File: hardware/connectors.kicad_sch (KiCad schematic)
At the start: 4 parts, among them J1 74650073R, J4 Conn_01x06, J5 UMPT-08-01-L-RA-WT-P-TR, J8 UMPT-08-01-L-RA-WT-P-TR

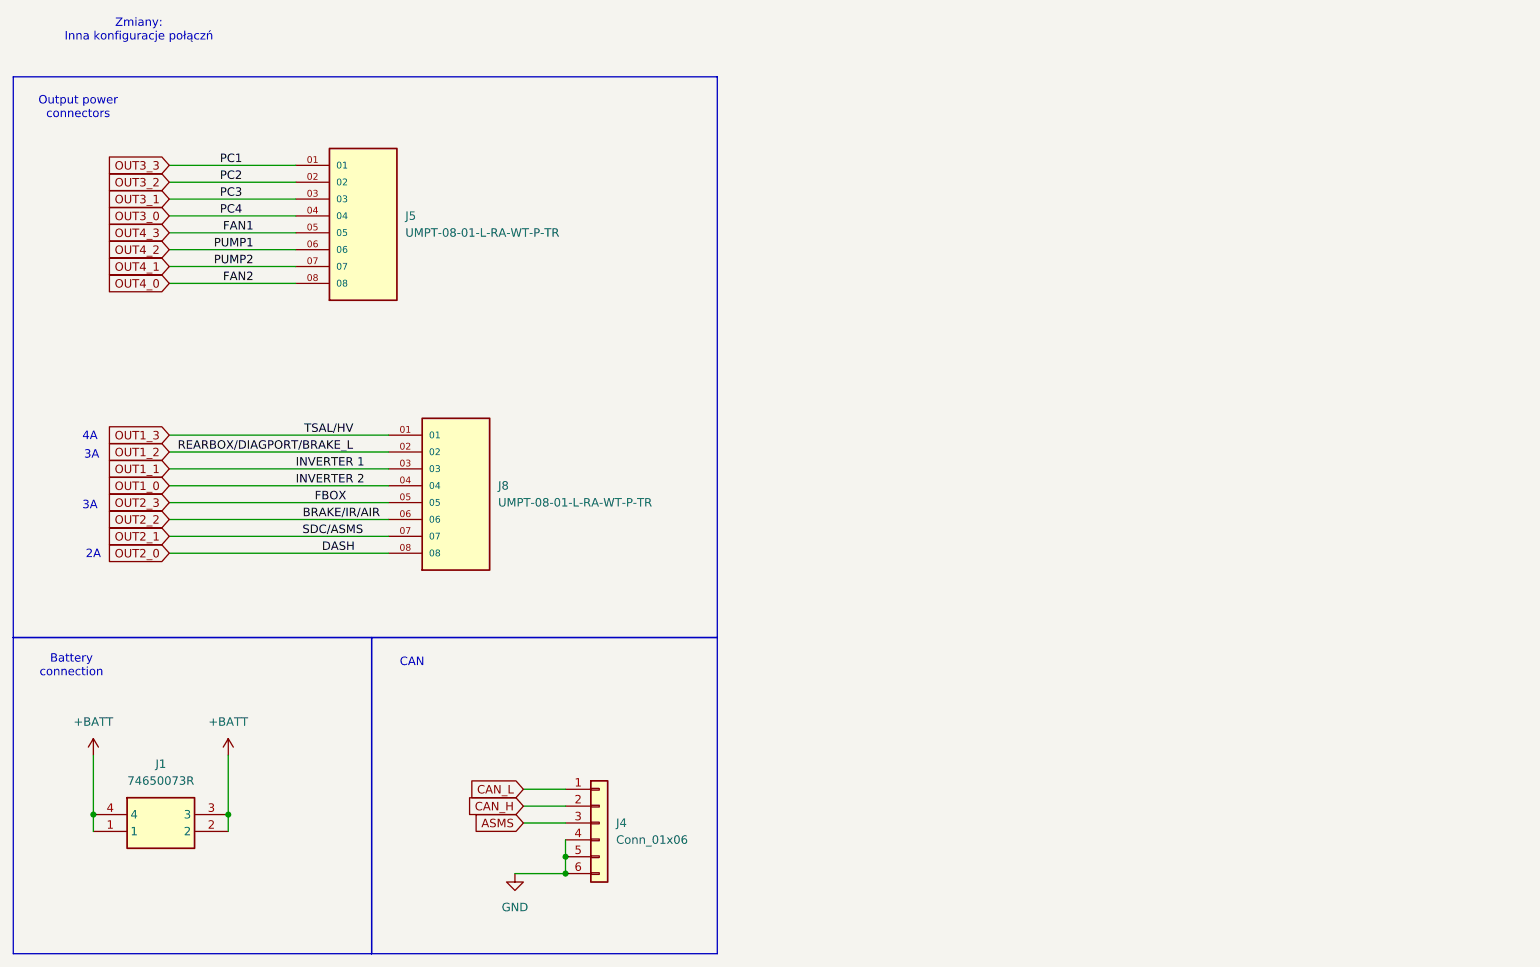
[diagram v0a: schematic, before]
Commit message: cube->cmake port, current calc fix, spi datalength fix, hard-v1.1.0 sync
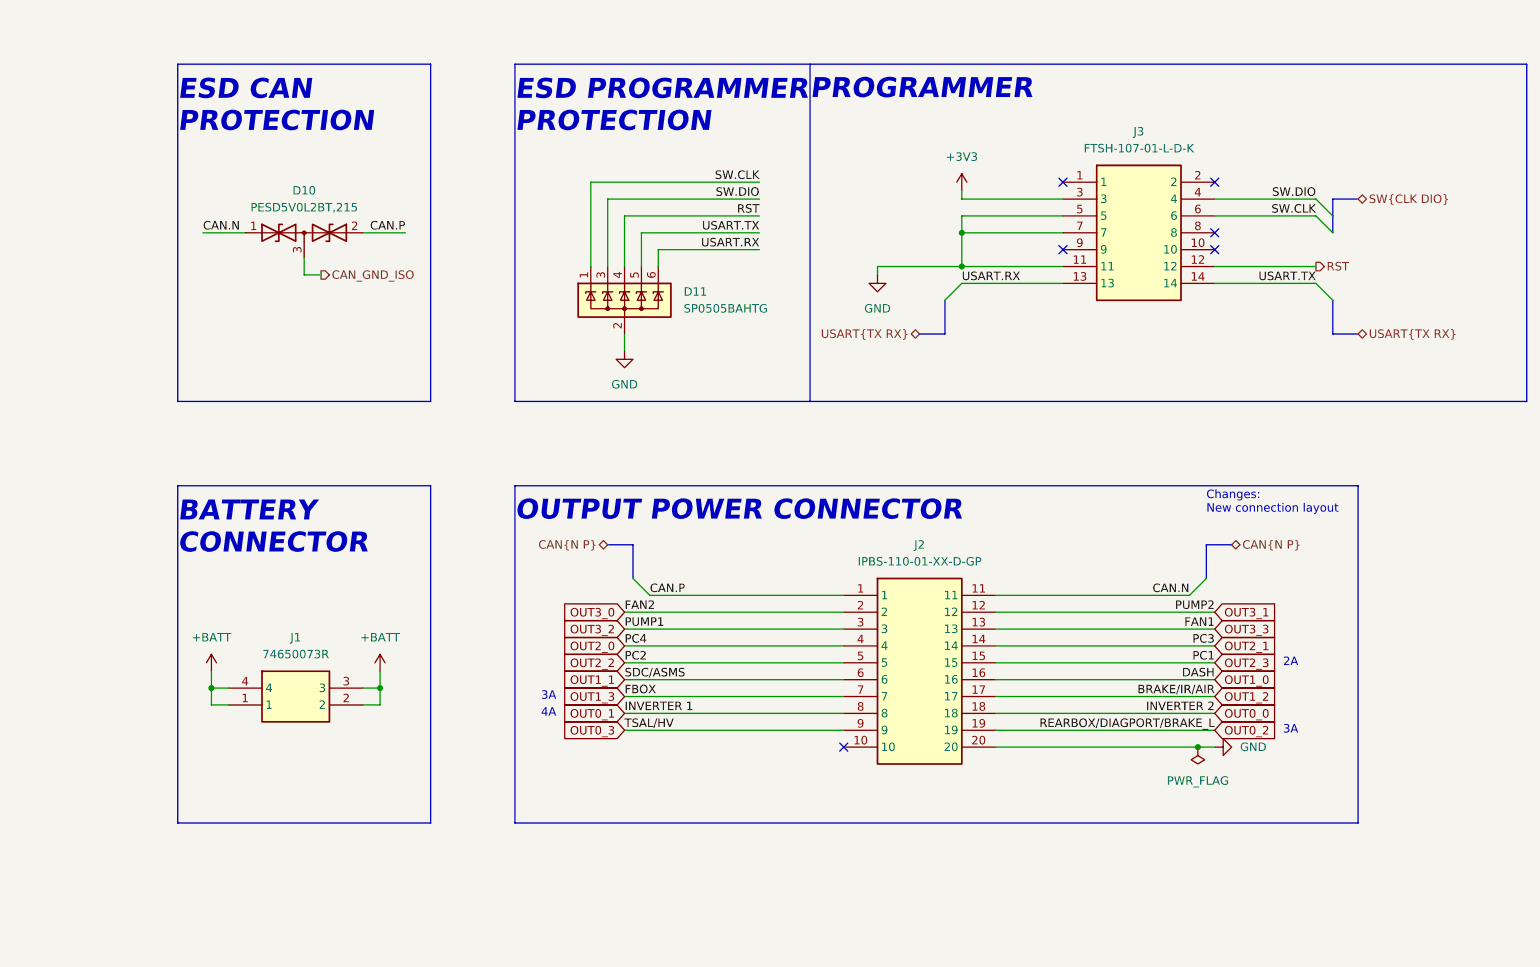
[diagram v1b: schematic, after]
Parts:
- removed J4: Conn_01x06, Connector_IDC:IDC-Header_2x03_P2.54mm_Vertical, symbol Connector_Generic:Conn_01x06
- removed J5, J8: UMPT-08-01-L-RA-WT-P-TR, UMPT-08-01-L-RA-WT-P-TR:SAMTEC_UMPT-08-01-L-RA-WT-P-TR, symbol UMPT-08-01-L-RA-WT-P-TR:UMPT-08-01-L-RA-WT-P-TR
- added D10: PESD5V0L2BT,215, Package_TO_SOT_SMD:SOT-23-3, symbol Device:D_TVS_Dual_AAC
- added D11: SP0505BAHTG, Package_TO_SOT_SMD:SOT-23-6_Handsoldering, symbol Power_Protection:SP0505BAHT
- added J2: IPBS-110-01-XX-D-GP, PDM:IPBT110H1TDRAGP, symbol PDM:IPBS-110-01-T-D-GP
- added J3: FTSH-107-01-L-D-K, PDM:FTSH-107-XX-YYY-D-K, symbol PDM:FTSH-107-01-L-D-K
- J1: footprint 74650073R -> PDM:74650073R; symbol Redcube_conn:74650073R -> PDM:74650073R; Done? (none) -> y
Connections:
- net GND: now also D11.2 (A), J2.20, J3.11, J3.5, J3.7
- net OUT1_0: now also J2.16
- net OUT1_1: now also J2.6
- net OUT1_2: now also J2.17
- net OUT1_3: now also J2.7
- net OUT2_0: now also J2.4
- net OUT2_1: now also J2.14
- net OUT2_2: now also J2.5
- net OUT2_3: now also J2.15
- net OUT3_0: now also J2.2
- net OUT3_1: now also J2.12
- net OUT3_2: now also J2.3
- net OUT3_3: now also J2.13
- new net +3V3: J3.3
- new net CAN.N: D10.1 (A1), J2.11
- new net CAN.P: D10.2 (A2), J2.1
- new net CAN_GND_ISO: D10.3 (common)
- new net OUT0_0: J2.18
- new net OUT0_1: J2.8
- new net OUT0_2: J2.19
- new net OUT0_3: J2.9
- new net RST: D11.4 (K), J3.12
- new net SW.CLK: D11.1 (K), J3.6
- new net SW.DIO: D11.3 (K), J3.4
- new net USART.RX: D11.6 (K), J3.13
- new net USART.TX: D11.5 (K), J3.14
- no-connect marks 0 -> 6
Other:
- note added: "BATTERY CONNECTOR"
- note added: "Changes: New connection layout"
- note added: "ESD CAN PROTECTION"
- note added: "ESD PROGRAMMER PROTECTION"
- note added: "OUTPUT POWER CONNECTOR"
- note added: "PROGRAMMER"
- note removed: "Battery connection"
- note removed: "CAN"
- note removed: "Output power connectors"
- note removed: "Zmiany: Inna konfiguracje połączń"
- company: (none) -> Authors: Grzegorz Potocki Jędrzej Kasprzyk
- title: (none) -> PDUv3
- moved on the sheet: J1
